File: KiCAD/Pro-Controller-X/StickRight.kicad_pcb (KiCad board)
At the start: 2 copper layers, 32.8 x 34 mm, 2 parts, among them J1 Conn_01x05_Pin

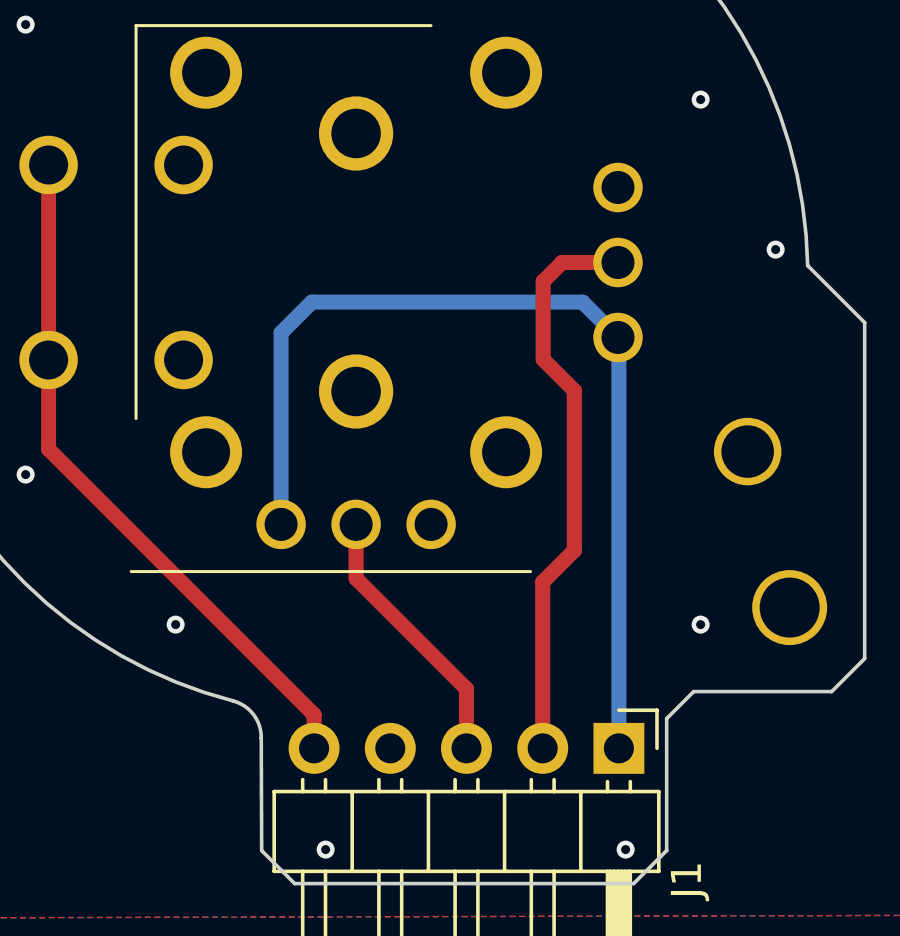
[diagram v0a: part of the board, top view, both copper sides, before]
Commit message: Rev 1.0.1 - Untested - Should fix reversal of right stick - no new output files
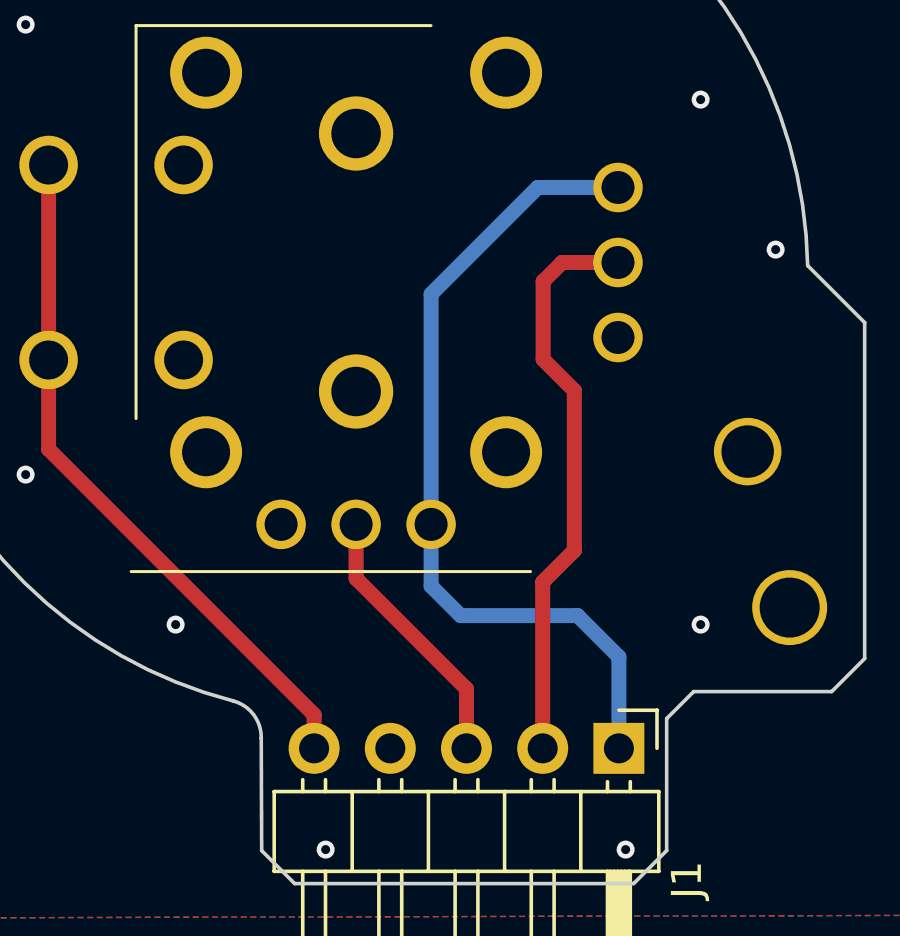
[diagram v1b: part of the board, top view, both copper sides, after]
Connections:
- U1 pad A11: Net-(J1-Pin_1) -> GND
- U1 pad A13: GND -> Net-(J1-Pin_1)
- U1 pad B11: Net-(J1-Pin_1) -> GND
- U1 pad B13: GND -> Net-(J1-Pin_1)
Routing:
- net Net-(J1-Pin_1): track 32.4 -> 27.9 mm
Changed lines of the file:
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@@
       (net 5 "GND") (pinfunction "A1") (pintype "input"))
     (pad "A11" thru_hole circle (at 2.7525 -6.627 90) (size 1.65 1.65) (drill 1.1) (layers "*.Cu" "*.Mask")
-      (net 1 "Net-(J1-Pin_1)") (pinfunction "A11") (pintype "input"))
+      (net 5 "GND") (pinfunction "A11") (pintype "input"))
     (pad "A12" thru_hole circle (at 0.2525 -6.627 90) (size 1.65 1.65) (drill 1.1) (layers "*.Cu" "*.Mask")
       (net 3 "Net-(J1-Pin_3)") (pinfunction "A12") (pintype "input"))
-    (pad "A13" thru_hole circle (at -2.2475 -6.627 90) (size 1.65 1.65) (drill 1.1) (layers "*.Cu" "*.Mask")
-      (net 5 "GND") (pinfunction "A13") (pintype "input"))
+    (pad "A13" thru_hole circle locked (at -2.2475 -6.627 90) (size 1.65 1.65) (drill 1.1) (layers "*.Cu" "*.Mask")
+      (net 1 "Net-(J1-Pin_1)") (pinfunction "A13") (pintype "input"))
     (pad "B1" thru_hole circle (at 10.5025 -1.147 90) (size 1.95 1.95) (drill 1.3) (layers "*.Cu" "*.Mask")
       (net 4 "Net-(J1-Pin_5)") (pinfunction "B1") (pintype "input"))
@@
     (pad "B3" thru_hole circle (at -12.8 -4.2 90) (size 2.25 2.25) (drill 1.75) (layers "*.Cu" "*.Mask"))
     (pad "B11" thru_hole circle (at -8.4775 -0.397 90) (size 1.65 1.65) (drill 1.1) (layers "*.Cu" "*.Mask")
-      (net 1 "Net-(J1-Pin_1)") (pinfunction "B11") (pintype "input"))
+      (net 5 "GND") (pinfunction "B11") (pintype "input"))
     (pad "B12" thru_hole circle (at -8.4775 2.103 90) (size 1.65 1.65) (drill 1.1) (layers "*.Cu" "*.Mask")
       (net 2 "Net-(J1-Pin_2)") (pinfunction "B12") (pintype "input"))
     (pad "B13" thru_hole circle (at -8.4775 4.603 90) (size 1.65 1.65) (drill 1.1) (layers "*.Cu" "*.Mask")
-      (net 5 "GND") (pinfunction "B13") (pintype "input"))
+      (net 1 "Net-(J1-Pin_1)") (pinfunction "B13") (pintype "input"))
     (pad "MH1" thru_hole circle (at -4.7475 -4.222 90) (size 2.4 2.4) (drill 1.6) (layers "*.Cu" "*.Mask")
       (net 5 "GND") (pinfunction "MH1") (pintype "input"))
@@
       (net 5 "GND") (pinfunction "MH2") (pintype "input"))
   )
-  (segment (start 137.04 81.75) (end 146.065 81.75) (width 0.5) (layer "B.Cu") (net 1))
-  (segment (start 147.275 96.625) (end 147.275 82.96) (width 0.5) (layer "B.Cu") (net 1))
-  (segment (start 146.065 81.75) (end 147.245 82.93) (width 0.5) (layer "B.Cu") (net 1))
-  (segment (start 136.015 82.775) (end 137.04 81.75) (width 0.5) (layer "B.Cu") (net 1))
-  (segment (start 136.015 89.16) (end 136.015 82.775) (width 0.5) (layer "B.Cu") (net 1))
-  (segment (start 147.275 82.96) (end 147.245 82.93) (width 0.5) (layer "B.Cu") (net 1))
+  (segment (start 141.015 89.16) (end 141.015 81.485) (width 0.5) (layer "B.Cu") (net 1))
+  (segment (start 145.9 92.2) (end 147.275 93.575) (width 0.5) (layer "B.Cu") (net 1))
+  (segment (start 147.275 93.575) (end 147.275 96.625) (width 0.5) (layer "B.Cu") (net 1))
+  (segment (start 141.015 81.485) (end 144.57 77.93) (width 0.5) (layer "B.Cu") (net 1))
+  (segment (start 144.57 77.93) (end 147.245 77.93) (width 0.5) (layer "B.Cu") (net 1))
+  (segment (start 142 92.2) (end 145.9 92.2) (width 0.5) (layer "B.Cu") (net 1))
+  (segment (start 141.015 89.16) (end 141.015 91.215) (width 0.5) (layer "B.Cu") (net 1))
   (segment (start 147.245 96.435) (end 147.135 96.545) (width 0.5) (layer "B.Cu") (net 1))
+  (segment (start 141.015 91.215) (end 142 92.2) (width 0.5) (layer "B.Cu") (net 1))
   (segment (start 144.75 81.06) (end 145.38 80.43) (width 0.5) (layer "F.Cu") (net 2))
   (segment (start 144.735 96.625) (end 144.735 91.085) (width 0.5) (layer "F.Cu") (net 2))
